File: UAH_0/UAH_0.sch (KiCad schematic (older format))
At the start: 64 parts, among them X17 Check_point, X18 Check_point, X2 Check_point, X3 Крепежное_отверстие_М3, X4 Крепежное_отверстие_М3, X5 Крепежное_отверстие_М3, X6 Крепежное_отверстие_М3, X7 LOGO_NIKITOS_19х7

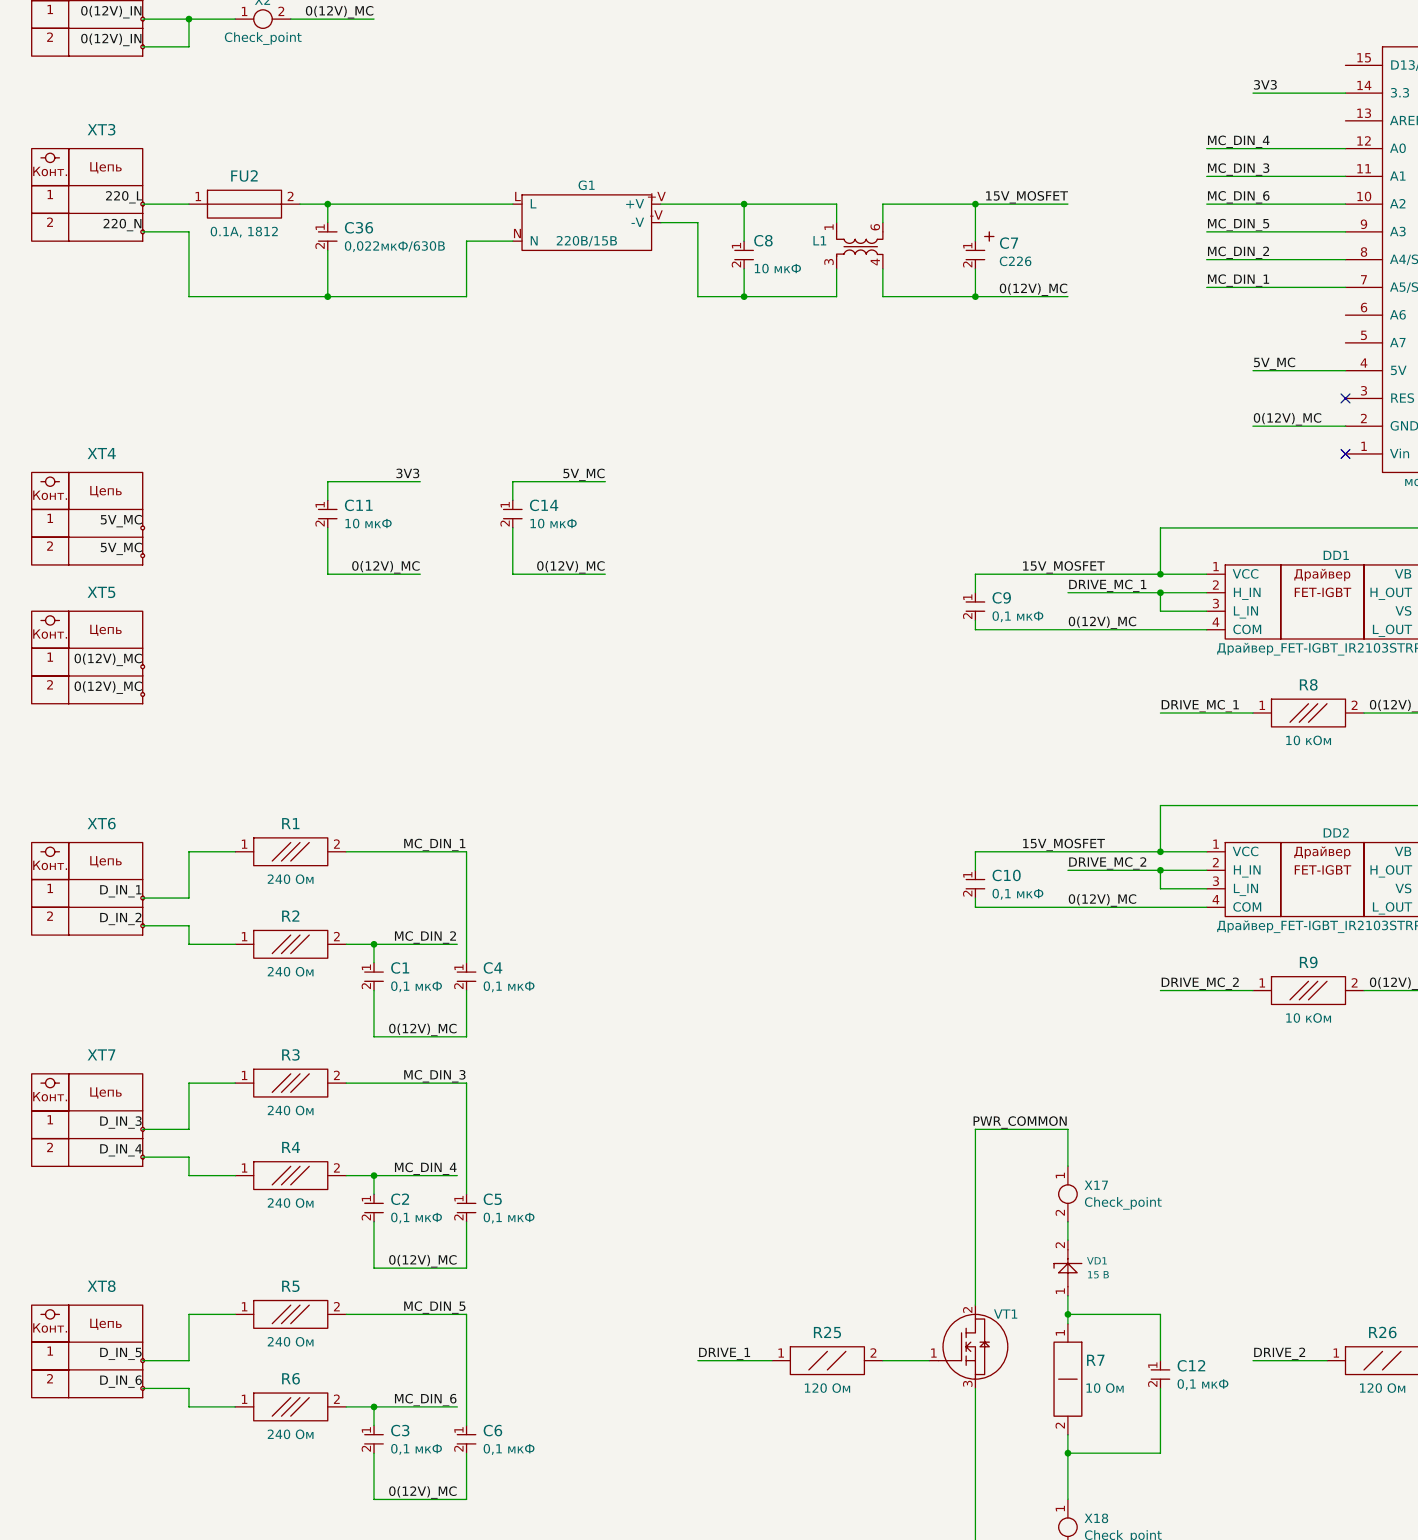
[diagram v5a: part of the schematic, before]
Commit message: добавлена маркировка, обновлены STEP, PDF, PNG, нет ЛОГО заказчика
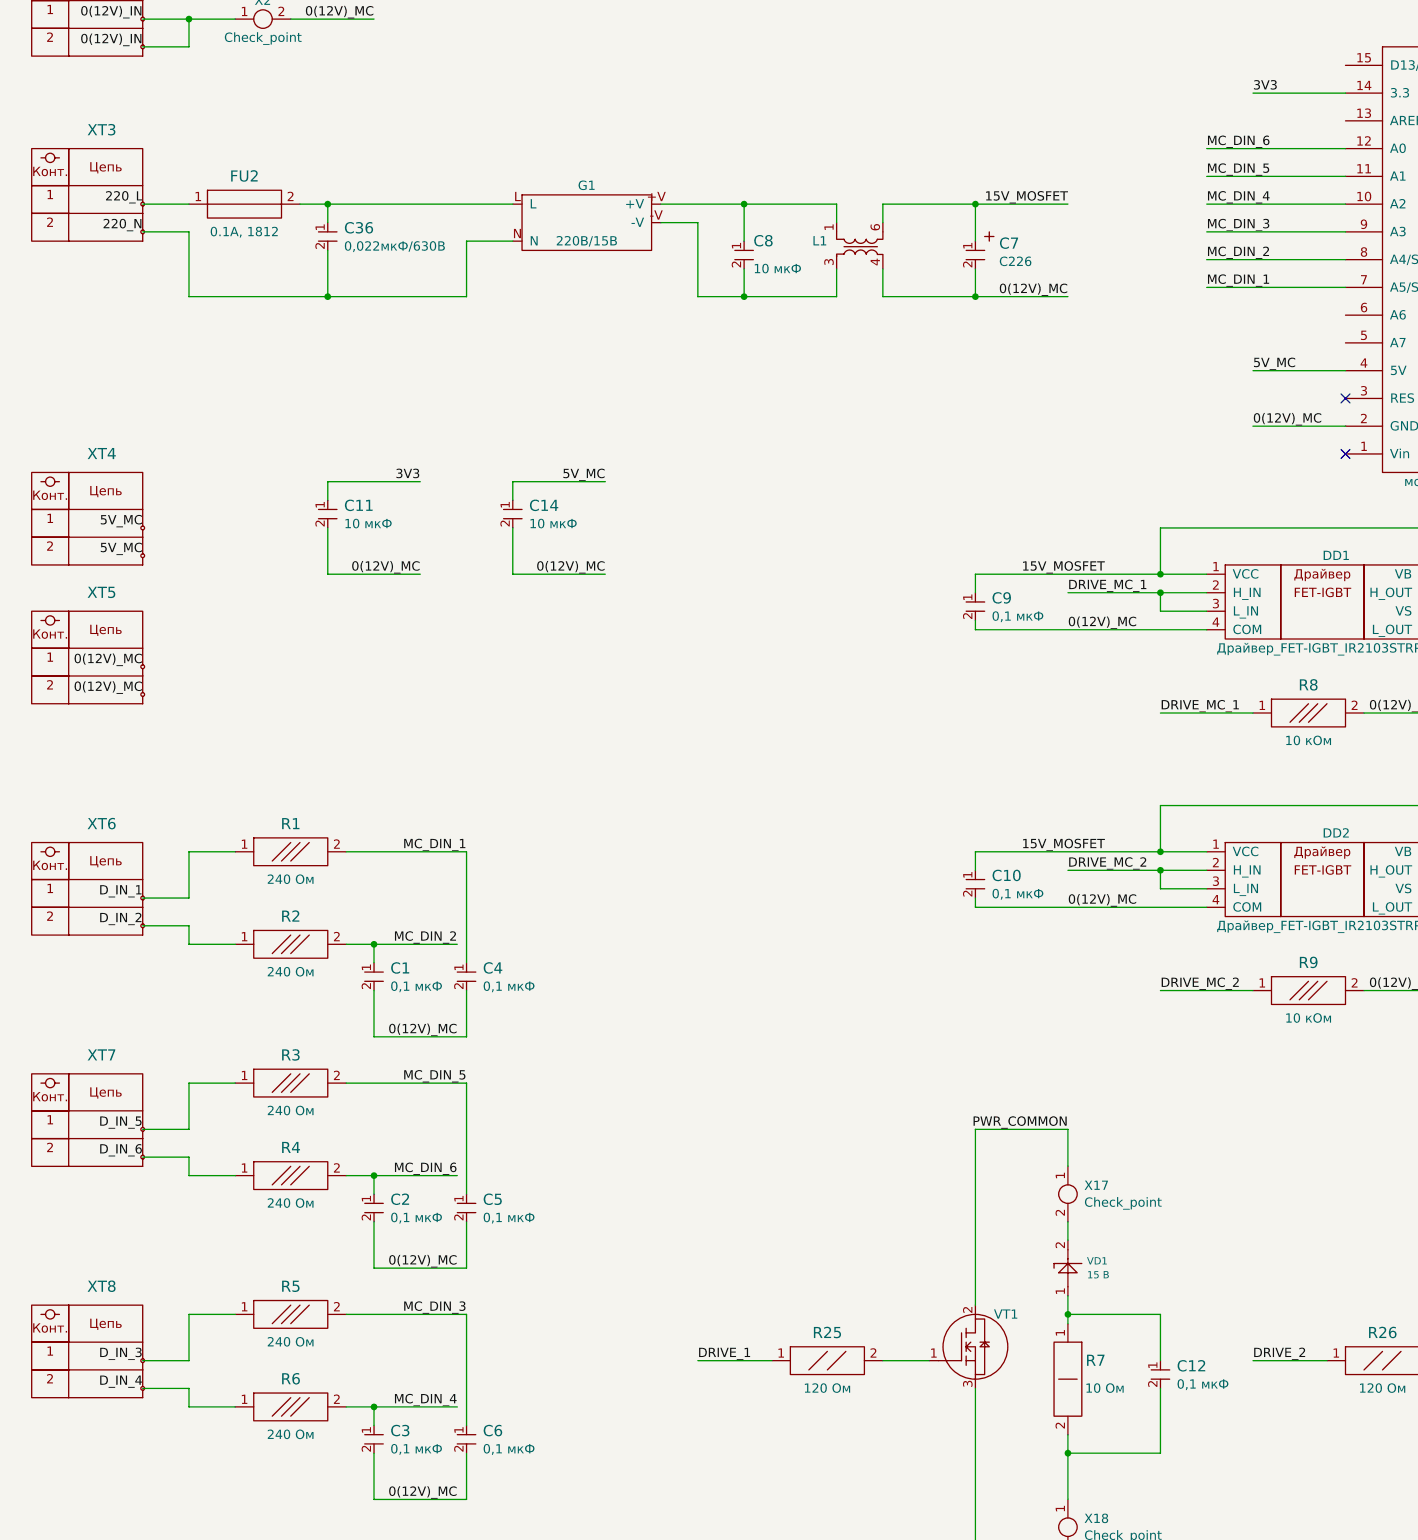
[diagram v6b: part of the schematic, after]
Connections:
- net D_IN_3: now also R5.1, XT8.1; no longer R3.1, XT7.1
- net D_IN_4: now also R6.1, XT8.2; no longer R4.1, XT7.2
- net D_IN_5: now also R3.1, XT7.1; no longer R5.1, XT8.1
- net D_IN_6: now also R4.1, XT7.2; no longer R6.1, XT8.2
- net MC_DIN_3: now also A1.9 (A3), C6.1, R5.2; no longer A1.11 (A1), C5.1, R3.2
- net MC_DIN_4: now also A1.10 (A2), C3.1, R6.2; no longer A1.12 (A0), C2.1, R4.2
- net MC_DIN_5: now also A1.11 (A1), C5.1, R3.2; no longer A1.9 (A3), C6.1, R5.2
- net MC_DIN_6: now also A1.12 (A0), C2.1, R4.2; no longer A1.10 (A2), C3.1, R6.2
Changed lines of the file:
@@
 	1    0    0    -1
 $EndComp
-Text Label 1500 8500 2    50   ~ 0
+Text Label 1500 9750 2    50   ~ 0
 D_IN_3
-Text Label 1500 8650 2    50   ~ 0
+Text Label 1500 9900 2    50   ~ 0
 D_IN_4
 $Comp
@@
 	1    0    0    -1
 $EndComp
-Text Label 1500 9750 2    50   ~ 0
+Text Label 1500 8500 2    50   ~ 0
 D_IN_5
-Text Label 1500 9900 2    50   ~ 0
+Text Label 1500 8650 2    50   ~ 0
 D_IN_6
 $Comp
@@
 Text Label 3200 9250 2    50   ~ 0
 0(12V)_MC
-Text Label 3250 8250 2    50   ~ 0
+Text Label 3250 9500 2    50   ~ 0
 MC_DIN_3
-Text Label 3200 8750 2    50   ~ 0
+Text Label 3200 10000 2    50   ~ 0
 MC_DIN_4
 Connection ~ 2750 8750
@@
 Text Label 3200 10500 2    50   ~ 0
 0(12V)_MC
-Text Label 3250 9500 2    50   ~ 0
+Text Label 3250 8250 2    50   ~ 0
 MC_DIN_5
-Text Label 3200 10000 2    50   ~ 0
-MC_DIN_6
 Connection ~ 2750 10000
 Wire Wire Line
@@
 Text Label 7250 3800 0    50   ~ 0
 MC_DIN_2
-Text Label 7250 3200 0    50   ~ 0
+Text Label 7250 3500 0    50   ~ 0
 MC_DIN_4
 Wire Wire Line
@@
 Wire Wire Line
 	7250 3500 8000 3500
-Text Label 7250 3500 0    50   ~ 0
+Text Label 7250 3200 0    50   ~ 0
 MC_DIN_6
+Text Label 7250 3350 0    50   ~ 0
+MC_DIN_5
+Wire Wire Line
+	7250 3800 8000 3800
 Text Label 7250 3650 0    50   ~ 0
-MC_DIN_5
-Wire Wire Line
-	7250 3800 8000 3800
-Text Label 7250 3350 0    50   ~ 0
 MC_DIN_3
 Wire Wire Line
@@
 NoConn ~ 8500 5800
 NoConn ~ 8500 7300
+Text Label 3200 8750 2    50   ~ 0
+MC_DIN_6
 $EndSCHEMATC

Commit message: UAH_0B, готова плата +gerbers
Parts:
- added X1: LOGO_NIKITOS_19х7, N_ICO:trinity_32x10, symbol elements_2020:LOGO_NIKITOS_19х7
- added X14: LOGO_NIKITOS_19х7, N_ICO:El-nikitos_QR_10x10, symbol elements_2020:LOGO_NIKITOS_19х7
- X7: footprint N_ICO:el-nikitos_19x7 -> N_ICO:ni_10x10
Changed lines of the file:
@@
 encoding utf-8
 Sheet 1 4
-Title ""
+Title "UAH.0B"
 Date ""
 Rev ""
@@
 F 0 "X7" H 12925 8625 50  0001 C CNN
 F 1 "LOGO_NIKITOS_19х7" H 12975 8400 50  0001 C CNN
-F 2 "N_ICO:el-nikitos_19x7" H 13000 8500 50  0001 C CNN
+F 2 "N_ICO:ni_10x10" H 13000 8500 50  0001 C CNN
 F 3 "" H 13000 8500 50  0001 C CNN
 F 4 "PCB_element" H 12975 8725 50  0001 C CNN "INFO"
@@
 Text Label 3200 8750 2    50   ~ 0
 MC_DIN_6
+$Comp
+L elements_2020:LOGO_NIKITOS_19х7 X1
+U 1 1 5F3ACBC9
+P 13000 9000
+F 0 "X1" H 12925 9125 50  0001 C CNN
+F 1 "LOGO_NIKITOS_19х7" H 12975 8900 50  0001 C CNN
+F 2 "N_ICO:trinity_32x10" H 13000 9000 50  0001 C CNN
+F 3 "" H 13000 9000 50  0001 C CNN
+F 4 "PCB_element" H 12975 9225 50  0001 C CNN "INFO"
+	1    13000 9000
+	1    0    0    -1
+$EndComp
+$Comp
+L elements_2020:LOGO_NIKITOS_19х7 X14
+U 1 1 5F3BDDEB
+P 13500 8500
+F 0 "X14" H 13425 8625 50  0001 C CNN
+F 1 "LOGO_NIKITOS_19х7" H 13475 8400 50  0001 C CNN
+F 2 "N_ICO:El-nikitos_QR_10x10" H 13500 8500 50  0001 C CNN
+F 3 "" H 13500 8500 50  0001 C CNN
+F 4 "PCB_element" H 13475 8725 50  0001 C CNN "INFO"
+	1    13500 8500
+	1    0    0    -1
+$EndComp
 $EndSCHEMATC

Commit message: в схеме отражены позиции для BOM
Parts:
- C1, C10, C12, C16, C2, C3, C4, C5, C6, C9: symbol MOTOR_2020_import:Конденсатор_16В_0.1_мкФ+-10проц. -> UAH_0-rescue:Конденсатор_16В_0.1_мкФ+-10проц.-MOTOR_2020_import; INFO 0,1 мкФ -> 0,1мкФ, 16В, 0603
- C11: value Конденсатор_16В_0.1_мкФ+-10проц. -> Конденсатор_16В_10_мкФ+-10проц.; symbol MOTOR_2020_import:Конденсатор_16В_0.1_мкФ+-10проц. -> UAH_0-rescue:Конденсатор_16В_0.1_мкФ+-10проц.-MOTOR_2020_import; INFO 10 мкФ -> 10 мкФ, 25В, 0603; LINK https://www.chipdip.ru/product0/9000591947 -> https://www.chipdip.ru/product/grm188r61e106m
- C13, C15: symbol MOTOR_2020_import:Конденсатор_16В_10_мкФ+-10проц. -> UAH_0-rescue:Конденсатор_16В_10_мкФ+-10проц.-MOTOR_2020_import; INFO 1 мкФ -> 1 мкФ, 50В, 0603; LINK https://www.chipdip.ru/product/grm21br61c106ke15l -> https://www.chipdip.ru/product0/226236018
- C14, C8: symbol MOTOR_2020_import:Конденсатор_16В_10_мкФ+-10проц. -> UAH_0-rescue:Конденсатор_16В_10_мкФ+-10проц.-MOTOR_2020_import; INFO 10 мкФ -> 10 мкФ, 25В, 0603; LINK https://www.chipdip.ru/product/grm21br61c106ke15l -> https://www.chipdip.ru/product/grm188r61e106m
- C36: symbol MOTOR_2020_components:Конденсатор_К10-83-25В-0,1_мкФ+-20проц. -> UAH_0-rescue:Конденсатор_К10-83-25В-0,1_мкФ+-20проц.-MOTOR_2020_components; INFO 0,022мкФ/630В -> 0,022мкФ, 630В, 1210
- C7: symbol MOTOR_2020_components:Конденсатор_К53-56А-32В-22_мкФ+-10проц. -> UAH_0-rescue:Конденсатор_К53-56А-32В-22_мкФ+-10проц.-MOTOR_2020_components; INFO (none) -> 22 мкФ, 20В, корпус D; LINK (none) -> https://www.chipdip.ru/product0/30090
- DD1, DD2: symbol elements_2020:Драйвер_FET-IGBT_IR2103STRPBF -> UAH_0-rescue:Драйвер_FET-IGBT_IR2103STRPBF-elements_2020; INFO (none) -> Драйвер, SO-8; LINK (none) -> https://www.chipdip.ru/product/ir2103strpbf
- FU1: INFO (none) -> 30А, 6.35х30; LINK (none) -> https://www.chipdip.ru/product/c630-abe-30a-250v
- FU2: symbol elements_2020:Предохранитель_MF-MSMF160_1,6А_1812 -> UAH_0-rescue:Предохранитель_MF-MSMF160_1,6А_1812-elements_2020; LINK (none) -> https://www.chipdip.ru/product/mf-msmf010
- G1: value AC-DC-преобразователь_IRM-10-15 -> AC-DC-преобразователь_IRM-05-15; symbol elements_2020:AC-DC-преобразователь_IRM-10-15 -> UAH_0-rescue:AC-DC-преобразователь_IRM-10-15-elements_2020; LINK https://www.chipdip.ru/product/irm-10-15 -> https://www.chipdip.ru/product/irm-05-15
- G2: INFO (none) -> 15В/5В, SOT223; LINK (none) -> https://www.chipdip.ru/product/lm1117gs-5.0
- L1: symbol elements_2020:Дроссель_B82731-T2451-A20_2х47мГн_0.45А_250В -> UAH_0-rescue:Дроссель_B82731-T2451-A20_2х47мГн_0.45А_250В-elements_2020; INFO (none) -> 2x47 мГн, 0.45А; LINK (none) -> https://www.chipdip.ru/product/b82731-t2451-a20
- R1, R2, R3, R4, R5, R6: symbol MOTOR_2020_components:Резистор_Р1-12-0,1_ум.-240_Ом±5%-Н-«А» -> UAH_0-rescue:Резистор_Р1-12-0,1_ум.-240_Ом±5%-Н-«А»-MOTOR_2020_components; INFO (none) -> 240 Ом, 0603; LINK (none) -> https://www.chipdip.ru/product0/9000079625
- R25, R26: symbol MOTOR_2020_components:Резистор_Р1-12-0,125-120_Ом±5%-Н-«А» -> UAH_0-rescue:Резистор_Р1-12-0,125-120_Ом±5%-Н-«А»-MOTOR_2020_components; INFO (none) -> 120 Ом, 0805; LINK (none) -> https://www.chipdip.ru/product0/9000079464
- R7: INFO 10 Ом -> 10 Ом, С1-4
- R8, R9: symbol MOTOR_2020_import:Резистор_10_кОм±5%_0,1Вт -> UAH_0-rescue:Резистор_10_кОм±5%_0,1Вт-MOTOR_2020_import; INFO 10 кОм -> 10 кОм, 0603
- VD1: symbol elements_2020:Стабилитрон_1N5352BRLG_вертикальный -> UAH_0-rescue:Стабилитрон_1N5352BRLG_вертикальный-elements_2020
- VD2: symbol elements_2020:Диод_VS-20ETS08S-M3 -> UAH_0-rescue:Диод_VS-20ETS08S-M3-elements_2020; INFO (none) -> 20А, 800В, D2PAK; LINK (none) -> https://www.chipdip.ru/product/vs-20ets08s-m3
- VT1, VT2: symbol elements_2020:MOSFET_N-канал_AUIRF3205Z -> UAH_0-rescue:MOSFET_N-канал_AUIRF3205Z-elements_2020; INFO (none) -> 75А, 55В, TO-220; LINK (none) -> https://www.chipdip.ru/product/auirf3205z
- X1, X14, X7: symbol elements_2020:LOGO_NIKITOS_19х7 -> UAH_0-rescue:LOGO_NIKITOS_19х7-elements_2020; LINK (none) -> -
- X17, X18, X2: symbol elements_2020:Check_point -> UAH_0-rescue:Check_point-elements_2020; INFO (none) -> PCB_element; LINK (none) -> -
- X3, X4, X5, X6: symbol MOTOR_2020_components:Крепежное_отверстие_М3 -> UAH_0-rescue:Крепежное_отверстие_М3-MOTOR_2020_components; LINK (none) -> -
- XT1, XT10, XT11, XT12, XT13, XT14, XT15, XT16, XT2, XT3, XT9: symbol elements_2020:Клеммник_х2_KLS2-300-5.00-02P-2S -> UAH_0-rescue:Клеммник_х2_KLS2-300-5.00-02P-2S-elements_2020; INFO (none) -> 15А, 5мм; LINK (none) -> https://www.chipdip.ru/product/dg301-5.0-02p-12
- XT4, XT5, XT6, XT7, XT8: symbol elements_2020:Клеммник_х2_KLS2-300-5.00-02P-2S -> UAH_0-rescue:Клеммник_х2_KLS2-300-5.00-02P-2S-elements_2020; INFO (none) -> 8А, 2.54мм; LINK (none) -> https://www.chipdip.ru/product/308-021-12-14
